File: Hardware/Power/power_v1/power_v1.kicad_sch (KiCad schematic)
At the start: 18 parts, among them J1 Conn_01x03, Q1 SIHF9Z24STRR-GE3, U1 LM3940

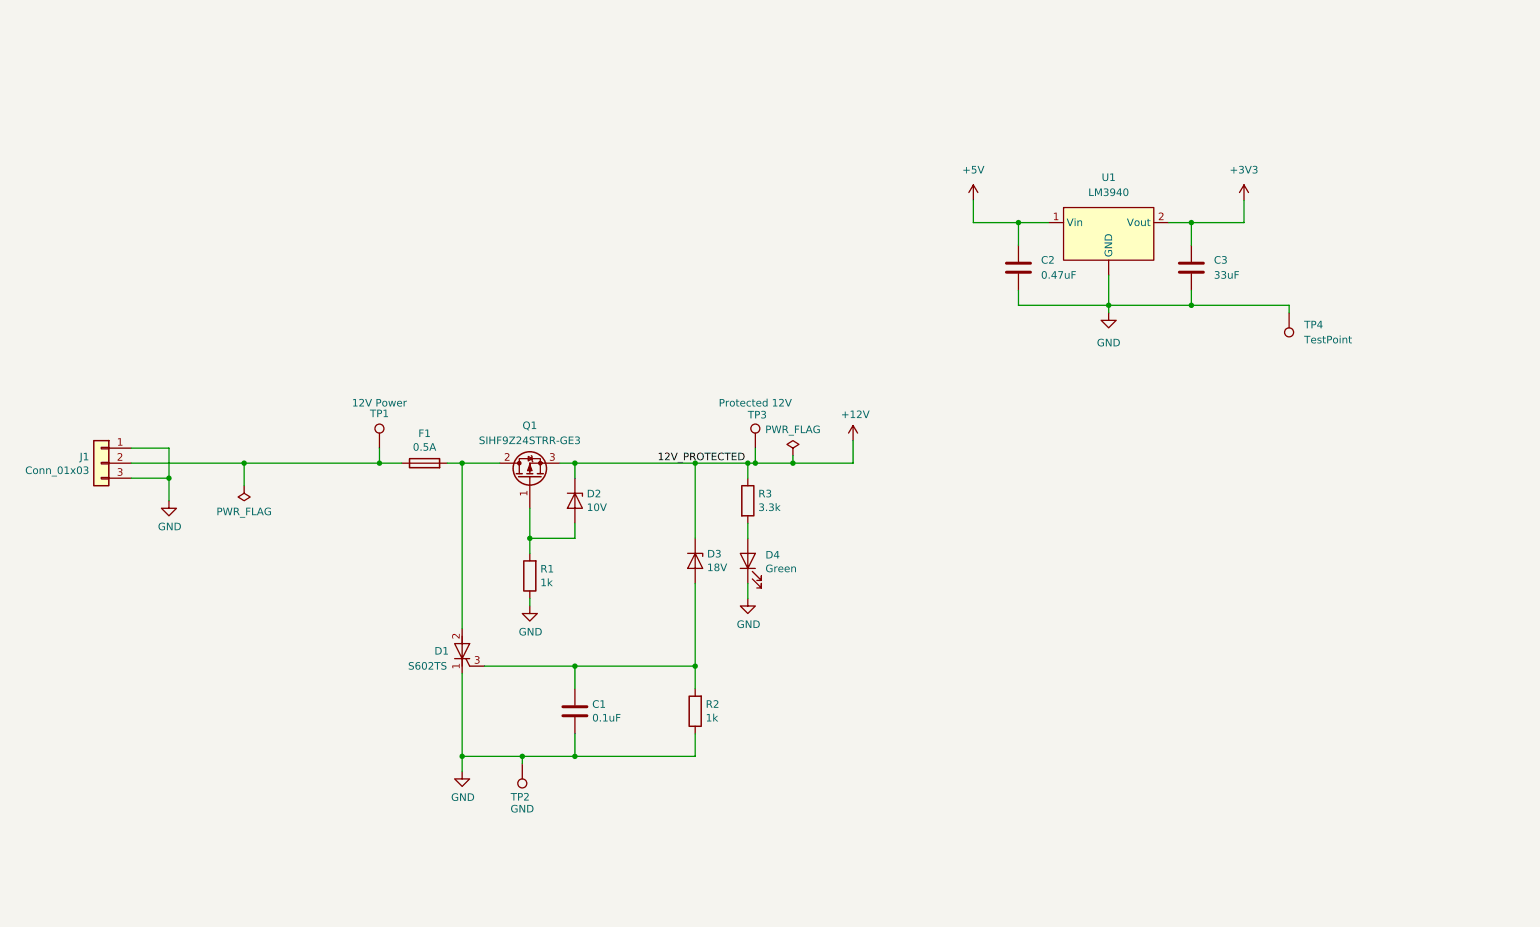
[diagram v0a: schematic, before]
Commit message: started 12 to 5V sch
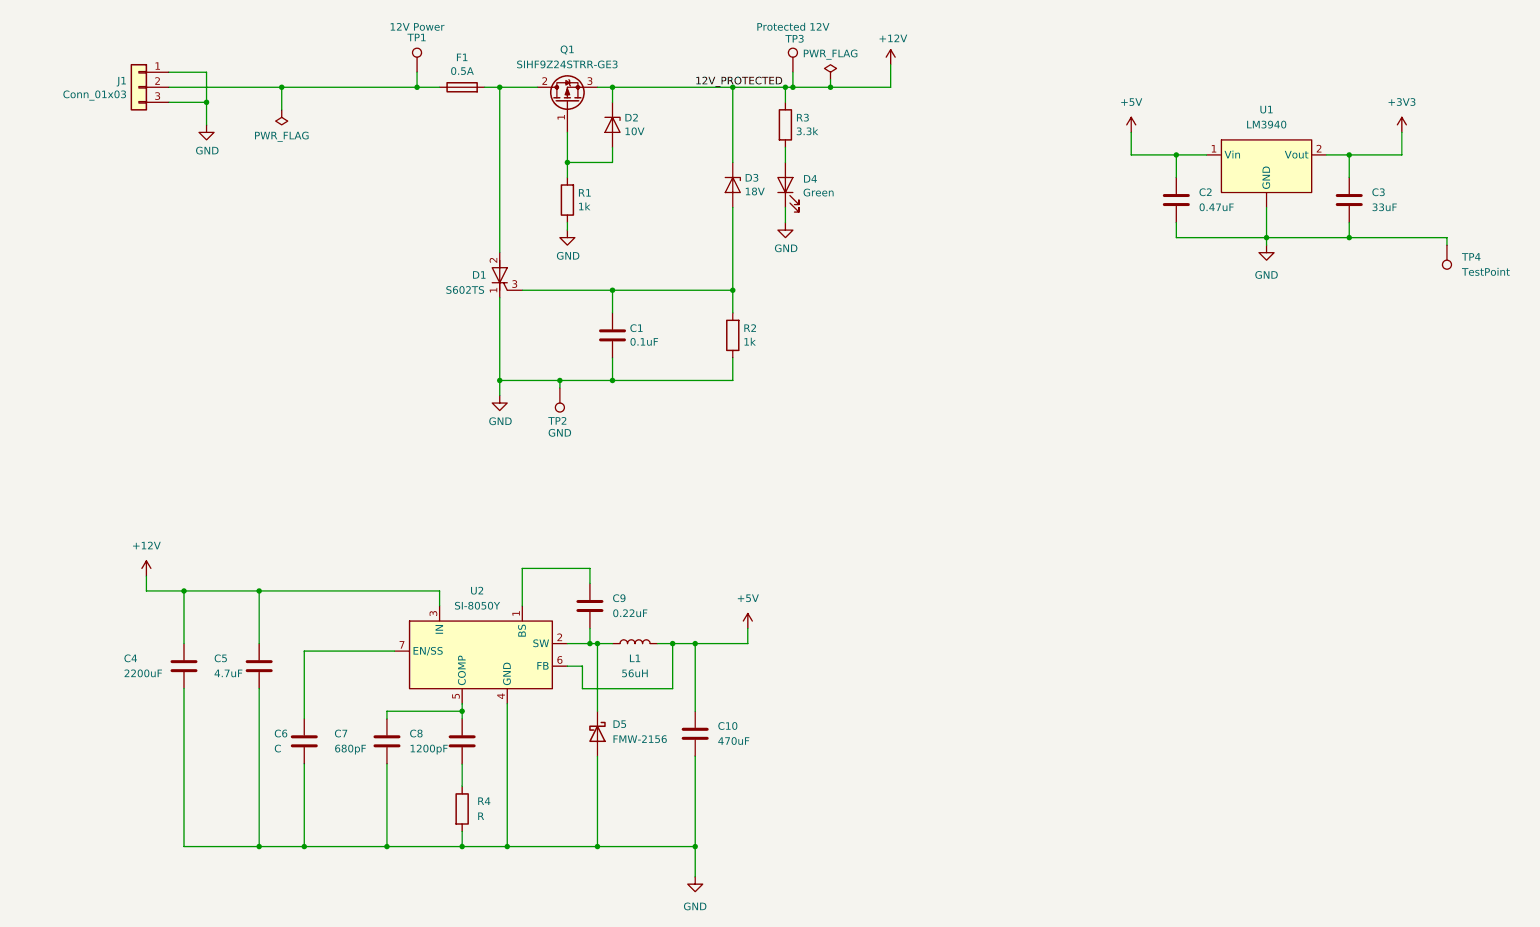
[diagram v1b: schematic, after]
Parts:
- added C10: 470uF, symbol Device:C
- added C4: 2200uF, symbol Device:C
- added C5: 4.7uF, symbol Device:C
- added C6: C, symbol Device:C
- added C7: 680pF, symbol Device:C
- added C8: 1200pF, symbol Device:C
- added C9: 0.22uF, symbol Device:C
- added D5: FMW-2156, symbol Device:D_Schottky
- added L1: 56uH, symbol Device:L
- added R4: R, symbol Device:R
- added U2: SI-8050Y, Package_TO_SOT_THT:TO-220F-7_P2.54x3.7mm_StaggerEven_Lead3.5mm_Vertical, symbol Backpack_buddy_libraries:SI-8050Y
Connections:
- net +12V: now also C4.1, C5.1, U2.3 (IN)
- net +5V: now also C10.1, L1.2, U2.6 (FB)
- net GND: now also C10.2, C4.2, C5.2, C6.2, C7.2, D5.2 (A), R4.2, U2.4 (GND)
- new net: C8.2, R4.1
- new net: C9.2, D5.1 (K), L1.1, U2.2 (SW)
- new net: C9.1, U2.1 (BS)
- new net: C7.1, C8.1, U2.5 (COMP)
- new net: C6.1, U2.7 (EN/SS)
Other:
- moved on the sheet: C1, C2, C3, D1, D2, D3, D4, F1, J1, Q1, R1, R2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

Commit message: progress on power circuit
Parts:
- removed C10: 470uF, symbol Device:C
- removed C4: 2200uF, symbol Device:C
- added C10: 470uF, Capacitor_THT:CP_Radial_D8.0mm_P3.50mm, symbol Device:C_Polarized
- added C4: 2200uF, Capacitor_THT:CP_Radial_D16.0mm_P7.50mm, symbol Device:C_Polarized
- added TP5: 5V, TestPoint:TestPoint_THTPad_D1.0mm_Drill0.5mm, symbol Connector:TestPoint
- C1: MPN CAP CER 0.1UF 35V X5R 0603 -> CAP CER 0.1UF 50V X7R 0603; Stock (none) -> https://www.digikey.com/en/products/detail/kemet/C0603C104K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
- C2: footprint (none) -> Capacitor_SMD:C_0603_1608Metric_Pad1.05x0.95mm_HandSolder; MPN (none) -> CAP CER 0.47UF 16V X7R 0603; Stock (none) -> https://www.digikey.com/en/products/detail/kemet/C0603X474J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
- C3: footprint (none) -> Capacitor_SMD:C_1206_3216Metric_Pad1.33x1.80mm_HandSolder; MPN (none) -> CAP CER 33UF 25V X5R 1206; Stock (none) -> https://www.digikey.com/en/products/detail/tdk-corporation/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
- C5: footprint (none) -> Capacitor_SMD:C_0805_2012Metric_Pad1.18x1.45mm_HandSolder; MPN (none) -> CAP CER 4.7UF 50V X5R 0805; Stock (none) -> https://www.digikey.com/en/products/detail/samsung-electro-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
- C7: footprint (none) -> Capacitor_SMD:C_0805_2012Metric_Pad1.18x1.45mm_HandSolder; MPN (none) -> CAP CER 680PF 200V X7R 0805; Stock (none) -> https://www.digikey.com/en/products/detail/kyocera-avx/0805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
- C8: footprint (none) -> Capacitor_SMD:C_0603_1608Metric_Pad1.05x0.95mm_HandSolder; MPN (none) -> CAP CER 1200PF 50V NP0 0805; Stock (none) -> https://www.digikey.com/en/products/detail/kyocera-avx/0805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
- C9: footprint (none) -> Capacitor_SMD:C_0603_1608Metric_Pad1.05x0.95mm_HandSolder; MPN (none) -> CAP CER 0.22UF 50V X7R 0603; Stock (none) -> https://www.digikey.com/en/products/detail/tdk-corporation/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
- D1: Stock (none) -> https://www.digikey.com/en/products/detail/littelfuse-inc/S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
- D2, D3: Stock (none) -> https://www.digikey.com/en/products/detail/nexperia-usa-inc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
- D4: value Green -> Red; MPN LED GREEN CLEAR 0603 SMD -> LED RED 0603 SMD; Stock (none) -> https://www.digikey.com/en/products/detail/rohm-semiconduct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
- D5: footprint (none) -> Package_TO_SOT_THT:TO-220-3_Vertical; MPN (none) -> FMW-2156; Note (none) -> Low stock!; Stock (none) -> https://www.digikey.com/en/products/detail/sanken/FMW-2156/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
- F1: Stock (none) -> https://www.digikey.com/en/products/detail/panasonic-electr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
- J1: Note LV Bus -> Battery Input; Stock (none) -> https://www.digikey.com/en/products/detail/molex/0022232031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
- Q1: Note (none) -> Substituted from original; Stock (none) -> https://www.digikey.com/en/products/detail/vishay-siliconix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
- R1, R2: MPN RES SMD 1K OHM 5% 1/4W 0603 -> RES SMD 1K OHM 1% 1/8W 0603; Note 0.1W 5% 0603 -> (none); Stock (none) -> https://www.digikey.com/en/products/detail/stackpole-electr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
- R3: MPN RES SMD 3.3K OHM 5% 1/4W 0603 -> RES SMD 3.3K OHM 5% 1/10W 0603; Stock (none) -> https://www.digikey.com/en/products/detail/yageo/RC0603JR-1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
- R4: value R -> 39k; footprint (none) -> Resistor_SMD:R_0603_1608Metric_Pad1.05x0.95mm_HandSolder; MPN (none) -> RES SMD 39K OHM 1% 1/10W 0603; Stock (none) -> https://www.digikey.com/en/products/detail/yageo/AC0603FR-0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
- TP1: DNP DNP -> (none); Note 12V Power -> 9V Power
- TP2: DNP DNP -> (none)
- TP3: DNP DNP -> (none); Note Protected 12V -> Protected 9V
- TP4: value TestPoint -> 3V3; footprint (none) -> TestPoint:TestPoint_THTPad_D1.0mm_Drill0.5mm
- U1: MPN (none) -> LM3940; Stock (none) -> Ordered!
- U2: MPN (none) -> SI-8050Y; Stock (none) -> Ordered!
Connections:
- net +3V3: now also TP4.1
- net +5V: now also C10.1, TP5.1
- net GND: now also C10.2, C4.2; no longer TP4.1
- net +12V renamed +9V
- net +9V: now also C4.1
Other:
- moved on the sheet: TP4

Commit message: created mcu symbol
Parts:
- TP3: value Protected 12V -> Protected 9V
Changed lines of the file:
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@@
       (effects (font (size 1.27 1.27)) (justify left top))
     )
-    (property "Value" "Protected 12V" (id 1) (at 139.7 27.94 0)
+    (property "Value" "Protected 9V" (id 1) (at 139.7 27.94 0)
       (effects (font (size 1.27 1.27)) (justify left) hide)
     )
@@
     )
     (path "/68ad6556-9956-45af-aca6-c9662c8c707b"
-      (reference "TP3") (unit 1) (value "Protected 12V") (footprint "TestPoint:TestPoint_THTPad_D1.0mm_Drill0.5mm")
+      (reference "TP3") (unit 1) (value "Protected 9V") (footprint "TestPoint:TestPoint_THTPad_D1.0mm_Drill0.5mm")
     )
     (path "/fc2f62c7-6aa4-448b-864e-c94828d41f5f"

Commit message: added LED indicators
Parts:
- added D6, D7: Red, LED_SMD:LED_0603_1608Metric_Pad1.05x0.95mm_HandSolder, symbol device:LED
- added R5, R6: 499, Resistor_SMD:R_0603_1608Metric_Pad1.05x0.95mm_HandSolder, symbol device:R
- R3: value 3.3k -> 1k; MPN RES SMD 3.3K OHM 5% 1/10W 0603 -> RES SMD 1K OHM 1% 1/8W 0603; Stock https://www.digikey.com/en/products/detail/yageo/RC0603JR-1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 -> https://www.digikey.com/en/products/detail/stackpole-electr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
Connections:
- net +3V3: now also R6.1
- net +5V: now also R5.1
- net GND: now also D6.1 (K), D7.1 (K)
- new net: D7.2 (A), R6.2
- new net: D6.2 (A), R5.2

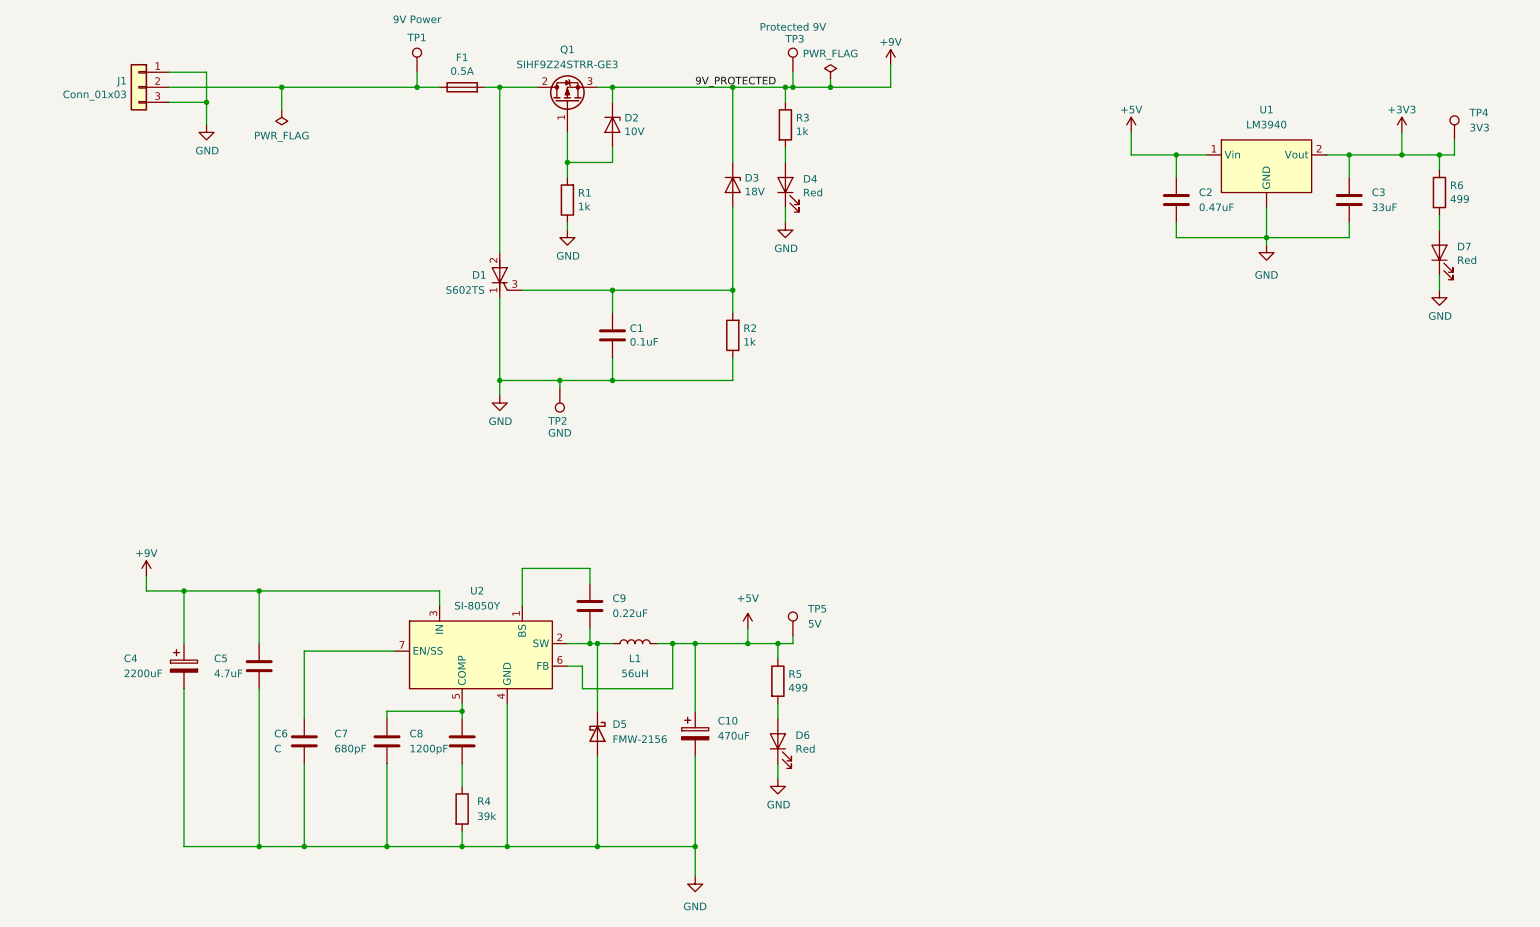
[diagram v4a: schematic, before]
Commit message: fixed all library issues and ERC errors
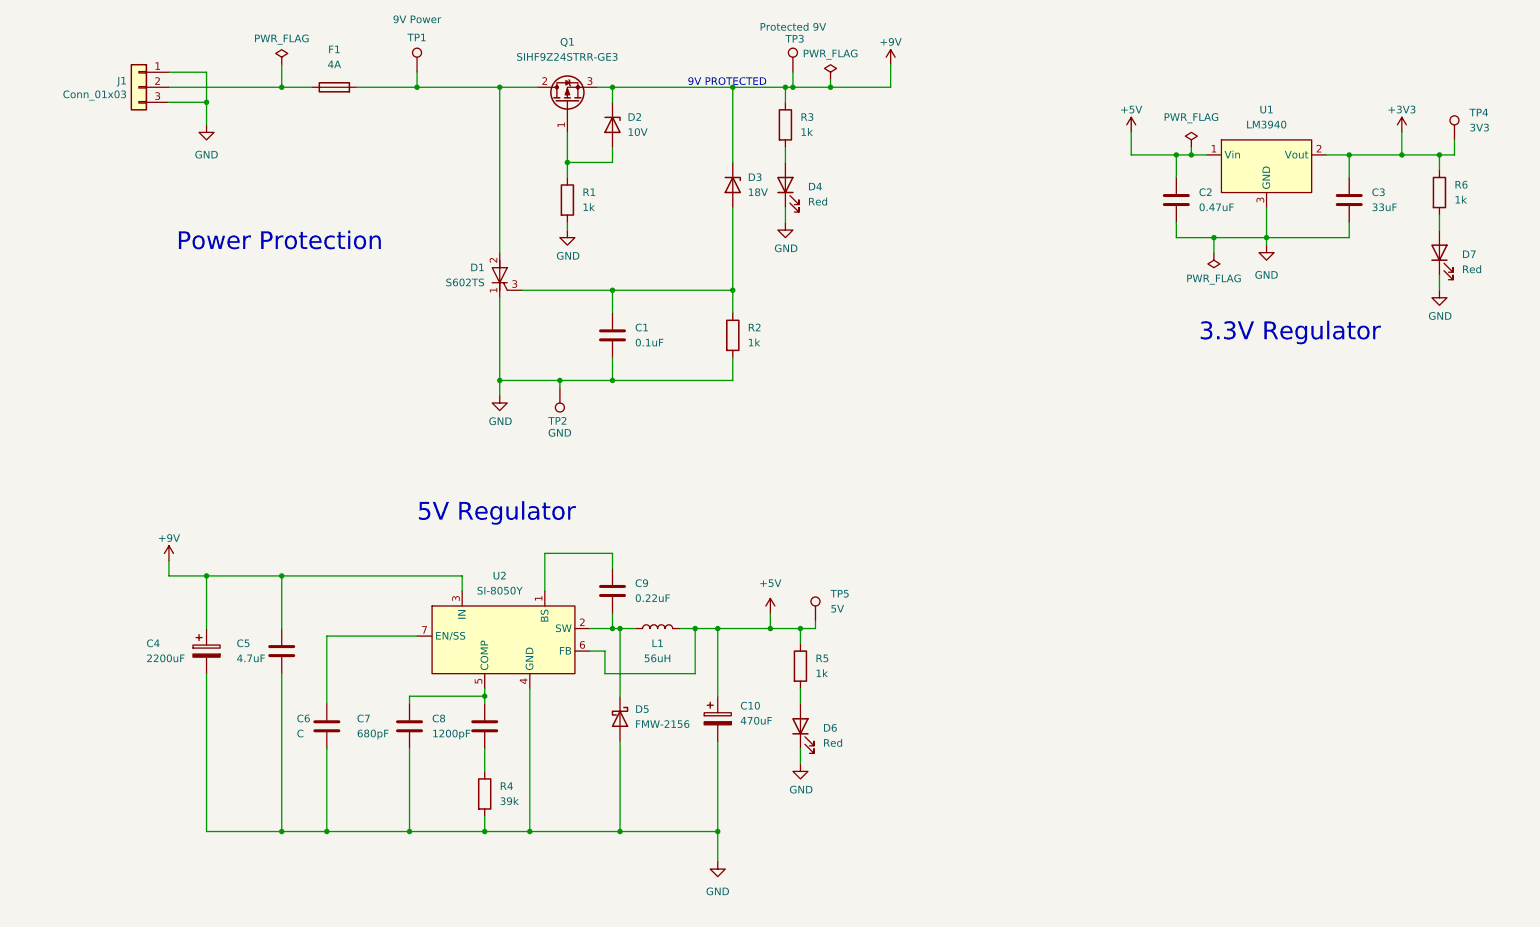
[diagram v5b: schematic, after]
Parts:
- removed C1: 0.1uF, Capacitor_SMD:C_0603_1608Metric_Pad1.05x0.95mm_HandSolder, symbol device:C
- removed D1: S602TS, Package_TO_SOT_SMD:SOT-223-3_TabPin2, symbol device:Q_SCR_KAG
- removed D2: 10V, Diode_SMD:D_SOD-123F, symbol device:D_Zener
- removed D3: 18V, Diode_SMD:D_SOD-123F, symbol device:D_Zener
- removed D4, D6, D7: Red, LED_SMD:LED_0603_1608Metric_Pad1.05x0.95mm_HandSolder, symbol device:LED
- removed F1: 0.5A, Fuse:Fuse_0603_1608Metric_Pad1.05x0.95mm_HandSolder, symbol device:Fuse
- removed Q1: SIHF9Z24STRR-GE3, Package_TO_SOT_SMD:TO-263-2, symbol device:Q_PMOS_GDS
- removed R1, R2, R3: 1k, Resistor_SMD:R_0603_1608Metric_Pad1.05x0.95mm_HandSolder, symbol device:R
- removed R5, R6: 499, Resistor_SMD:R_0603_1608Metric_Pad1.05x0.95mm_HandSolder, symbol device:R
- added C1: 0.1uF, Capacitor_SMD:C_0603_1608Metric_Pad1.05x0.95mm_HandSolder, symbol Device:C
- added D1: S602TS, Package_TO_SOT_SMD:SOT-223-3_TabPin2, symbol Device:Q_SCR_KAG
- added D2: 10V, Diode_SMD:D_SOD-123F, symbol Device:D_Zener
- added D3: 18V, Diode_SMD:D_SOD-123F, symbol Device:D_Zener
- added D4, D6, D7: Red, LED_SMD:LED_0603_1608Metric_Pad1.05x0.95mm_HandSolder, symbol Device:LED
- added F1: 4A, symbol Device:Fuse
- added Q1: SIHF9Z24STRR-GE3, Package_TO_SOT_SMD:TO-263-2, symbol Device:Q_PMOS_GDS
- added R1, R2, R3, R5, R6: 1k, Resistor_SMD:R_0603_1608Metric_Pad1.05x0.95mm_HandSolder, symbol Device:R
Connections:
- net +3V3: now also R6.1
- net +5V: now also R5.1
- net +9V: now also D2.1 (K), D3.1 (K), Q1.3 (S), R3.1
- net GND: now also U1.3 (GND), C1.2, D1.1 (K), D4.1 (K), D6.1 (K), D7.1 (K), R1.2, R2.2; no longer U1. (GND)
- net at J1.2 (Pin_2): now also F1.1; no longer TP1.1
- new net: D6.2 (A), R5.2
- new net: D1.2 (A), F1.2, Q1.2 (D), TP1.1
- new net: C1.1, D1.3 (G), D3.2 (A), R2.1
- new net: D4.2 (A), R3.2
- new net: D7.2 (A), R6.2
- new net: D2.2 (A), Q1.1 (G), R1.1
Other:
- note added: "3.3V Regulator"
- note added: "5V Regulator"
- note added: "9V PROTECTED"
- note added: "Power Protection"
- moved on the sheet: C10, C4, C5, C6, C7, C8, C9, D5, L1, R4, TP5
